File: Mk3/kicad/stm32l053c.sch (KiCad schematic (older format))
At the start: 24 parts, among them J1 CONN_01X02, P1 SWD, U1 AP2112, U2 STM32L053C8_LQFP48, U3 ADS1015, U4 EDGE_SMA, U5 RFM92/95

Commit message: Solar power
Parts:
- removed R5: R_Shunt, symbol R_Shunt
- added R?: R, symbol R
- D2: footprint (none) -> Diodes_SMD:D_0805
- J1, SC1: footprint (none) -> Pin_Headers:Pin_Header_Straight_1x02_Pitch2.54mm
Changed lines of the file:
@@
 $EndDescr
 $Comp
-L Earth #PWR5
+L Earth #PWR01
 U 1 1 58021BE1
 P 6425 1775
-F 0 "#PWR5" H 6425 1525 50  0001 C CNN
+F 0 "#PWR01" H 6425 1525 50  0001 C CNN
 F 1 "Earth" H 6425 1625 50  0001 C CNN
 F 2 "" H 6425 1775 50  0000 C CNN
@@
 $EndComp
 $Comp
-L GNDA #PWR19
+L GNDA #PWR02
 U 1 1 58021F75
 P 9325 5925
-F 0 "#PWR19" H 9325 5675 50  0001 C CNN
+F 0 "#PWR02" H 9325 5675 50  0001 C CNN
 F 1 "GNDA" H 9325 5775 50  0000 C CNN
 F 2 "" H 9325 5925 50  0000 C CNN
@@
 $EndComp
 $Comp
-L Earth #PWR20
+L Earth #PWR03
 U 1 1 58021F89
 P 9825 5925
-F 0 "#PWR20" H 9825 5675 50  0001 C CNN
+F 0 "#PWR03" H 9825 5675 50  0001 C CNN
 F 1 "Earth" H 9825 5775 50  0001 C CNN
 F 2 "" H 9825 5925 50  0000 C CNN
@@
 $EndComp
 $Comp
-L GNDA #PWR21
+L GNDA #PWR04
 U 1 1 58022154
 P 8175 5950
-F 0 "#PWR21" H 8175 5700 50  0001 C CNN
+F 0 "#PWR04" H 8175 5700 50  0001 C CNN
 F 1 "GNDA" H 8175 5800 50  0000 C CNN
 F 2 "" H 8175 5950 50  0000 C CNN
@@
 $EndComp
 $Comp
-L Earth #PWR22
+L Earth #PWR05
 U 1 1 580221FA
 P 8675 5950
-F 0 "#PWR22" H 8675 5700 50  0001 C CNN
+F 0 "#PWR05" H 8675 5700 50  0001 C CNN
 F 1 "Earth" H 8675 5800 50  0001 C CNN
 F 2 "" H 8675 5950 50  0000 C CNN
@@
 $EndComp
 $Comp
-L Earth #PWR10
+L Earth #PWR06
 U 1 1 580369A9
 P 2425 3075
-F 0 "#PWR10" H 2425 2825 50  0001 C CNN
+F 0 "#PWR06" H 2425 2825 50  0001 C CNN
 F 1 "Earth" H 2425 2925 50  0001 C CNN
 F 2 "" H 2425 3075 50  0000 C CNN
@@
 PA0
 $Comp
-L Earth #PWR7
+L Earth #PWR07
 U 1 1 58039244
 P 7525 1775
-F 0 "#PWR7" H 7525 1525 50  0001 C CNN
+F 0 "#PWR07" H 7525 1525 50  0001 C CNN
 F 1 "Earth" H 7525 1625 50  0001 C CNN
 F 2 "" H 7525 1775 50  0000 C CNN
@@
 $EndComp
 $Comp
-L Earth #PWR6
+L Earth #PWR08
 U 1 1 5803BDC8
 P 7075 1775
-F 0 "#PWR6" H 7075 1525 50  0001 C CNN
+F 0 "#PWR08" H 7075 1525 50  0001 C CNN
 F 1 "Earth" H 7075 1625 50  0001 C CNN
 F 2 "" H 7075 1775 50  0000 C CNN
@@
 $EndComp
 $Comp
-L Earth #PWR16
+L Earth #PWR09
 U 1 1 58065816
 P 7275 4950
-F 0 "#PWR16" H 7275 4700 50  0001 C CNN
+F 0 "#PWR09" H 7275 4700 50  0001 C CNN
 F 1 "Earth" H 7275 4800 50  0001 C CNN
 F 2 "" H 7275 4950 50  0000 C CNN
@@
 $EndComp
 $Comp
-L Earth #PWR11
+L Earth #PWR010
 U 1 1 58077163
 P 3575 3075
-F 0 "#PWR11" H 3575 2825 50  0001 C CNN
+F 0 "#PWR010" H 3575 2825 50  0001 C CNN
 F 1 "Earth" H 3575 2925 50  0001 C CNN
 F 2 "" H 3575 3075 50  0000 C CNN
@@
 $EndComp
 $Comp
-L Earth #PWR18
+L Earth #PWR011
 U 1 1 592DF55A
 P 2625 5475
-F 0 "#PWR18" H 2625 5225 50  0001 C CNN
+F 0 "#PWR011" H 2625 5225 50  0001 C CNN
 F 1 "Earth" H 2625 5325 50  0001 C CNN
 F 2 "" H 2625 5475 50  0000 C CNN
@@
 NoConn ~ 4150 1625
 $Comp
-L Earth #PWR8
+L Earth #PWR012
 U 1 1 592F1C89
 P 3750 1925
-F 0 "#PWR8" H 3750 1675 50  0001 C CNN
+F 0 "#PWR012" H 3750 1675 50  0001 C CNN
 F 1 "Earth" H 3750 1775 50  0001 C CNN
 F 2 "" H 3750 1925 50  0000 C CNN
@@
 RFM_RST
 $Comp
-L +3.3V #PWR1
+L +3.3V #PWR013
 U 1 1 592F43A5
 P 4450 1175
-F 0 "#PWR1" H 4450 1025 50  0001 C CNN
+F 0 "#PWR013" H 4450 1025 50  0001 C CNN
 F 1 "+3.3V" H 4450 1315 50  0000 C CNN
 F 2 "" H 4450 1175 50  0001 C CNN
@@
 $EndComp
 $Comp
-L +3.3V #PWR9
+L +3.3V #PWR014
 U 1 1 592F4BC3
 P 1925 2875
-F 0 "#PWR9" H 1925 2725 50  0001 C CNN
+F 0 "#PWR014" H 1925 2725 50  0001 C CNN
 F 1 "+3.3V" H 1925 3015 50  0000 C CNN
 F 2 "" H 1925 2875 50  0001 C CNN
@@
 $EndComp
 $Comp
-L +3.3V #PWR2
+L +3.3V #PWR015
 U 1 1 592F4E66
 P 8475 1425
-F 0 "#PWR2" H 8475 1275 50  0001 C CNN
+F 0 "#PWR015" H 8475 1275 50  0001 C CNN
 F 1 "+3.3V" H 8475 1565 50  0000 C CNN
 F 2 "" H 8475 1425 50  0001 C CNN
@@
 $EndComp
 $Comp
-L +3.3V #PWR26
+L +3.3V #PWR016
 U 1 1 592F53D7
 P 4775 6725
-F 0 "#PWR26" H 4775 6575 50  0001 C CNN
+F 0 "#PWR016" H 4775 6575 50  0001 C CNN
 F 1 "+3.3V" H 4775 6865 50  0000 C CNN
 F 2 "" H 4775 6725 50  0001 C CNN
@@
 $EndComp
 $Comp
-L +3.3V #PWR3
+L +3.3V #PWR017
 U 1 1 592F54CD
 P 7525 1475
-F 0 "#PWR3" H 7525 1325 50  0001 C CNN
+F 0 "#PWR017" H 7525 1325 50  0001 C CNN
 F 1 "+3.3V" H 7525 1615 50  0000 C CNN
 F 2 "" H 7525 1475 50  0001 C CNN
@@
 NoConn ~ 3400 7025
 $Comp
-L Earth #PWR27
+L Earth #PWR018
 U 1 1 592F7C8A
 P 4775 7025
-F 0 "#PWR27" H 4775 6775 50  0001 C CNN
+F 0 "#PWR018" H 4775 6775 50  0001 C CNN
 F 1 "Earth" H 4775 6875 50  0001 C CNN
 F 2 "" H 4775 7025 50  0000 C CNN
@@
 $EndComp
 $Comp
-L Earth #PWR23
+L Earth #PWR019
 U 1 1 592F7CF0
 P 2750 6425
-F 0 "#PWR23" H 2750 6175 50  0001 C CNN
+F 0 "#PWR019" H 2750 6175 50  0001 C CNN
 F 1 "Earth" H 2750 6275 50  0001 C CNN
 F 2 "" H 2750 6425 50  0000 C CNN
@@
 $EndComp
 $Comp
-L Earth #PWR28
+L Earth #PWR020
 U 1 1 592F7EE4
 P 3225 7125
-F 0 "#PWR28" H 3225 6875 50  0001 C CNN
+F 0 "#PWR020" H 3225 6875 50  0001 C CNN
 F 1 "Earth" H 3225 6975 50  0001 C CNN
 F 2 "" H 3225 7125 50  0000 C CNN
@@
 $EndComp
 $Comp
-L Earth #PWR24
+L Earth #PWR021
 U 1 1 592F80DC
 P 1300 6575
-F 0 "#PWR24" H 1300 6325 50  0001 C CNN
+F 0 "#PWR021" H 1300 6325 50  0001 C CNN
 F 1 "Earth" H 1300 6425 50  0001 C CNN
 F 2 "" H 1300 6575 50  0000 C CNN
@@
 $EndComp
 $Comp
-L Earth #PWR25
+L Earth #PWR022
 U 1 1 592F814F
 P 2050 6600
-F 0 "#PWR25" H 2050 6350 50  0001 C CNN
+F 0 "#PWR022" H 2050 6350 50  0001 C CNN
 F 1 "Earth" H 2050 6450 50  0001 C CNN
 F 2 "" H 2050 6600 50  0000 C CNN
@@
 $EndComp
 $Comp
-L Earth #PWR17
+L Earth #PWR023
 U 1 1 59301904
 P 3525 5175
-F 0 "#PWR17" H 3525 4925 50  0001 C CNN
+F 0 "#PWR023" H 3525 4925 50  0001 C CNN
 F 1 "Earth" H 3525 5025 50  0001 C CNN
 F 2 "" H 3525 5175 50  0000 C CNN
@@
 $EndComp
 $Comp
-L Earth #PWR15
+L Earth #PWR024
 U 1 1 593024E3
 P 3425 4475
-F 0 "#PWR15" H 3425 4225 50  0001 C CNN
+F 0 "#PWR024" H 3425 4225 50  0001 C CNN
 F 1 "Earth" H 3425 4325 50  0001 C CNN
 F 2 "" H 3425 4475 50  0000 C CNN
@@
 $EndComp
 $Comp
-L +3.3V #PWR12
+L +3.3V #PWR025
 U 1 1 59303669
 P 2625 4175
-F 0 "#PWR12" H 2625 4025 50  0001 C CNN
+F 0 "#PWR025" H 2625 4025 50  0001 C CNN
 F 1 "+3.3V" H 2625 4315 50  0000 C CNN
 F 2 "" H 2625 4175 50  0001 C CNN
@@
 $EndComp
 $Comp
-L +3.3V #PWR13
+L +3.3V #PWR026
 U 1 1 59303771
 P 3825 4175
-F 0 "#PWR13" H 3825 4025 50  0001 C CNN
+F 0 "#PWR026" H 3825 4025 50  0001 C CNN
 F 1 "+3.3V" H 3825 4315 50  0000 C CNN
 F 2 "" H 3825 4175 50  0001 C CNN
@@
 $EndComp
 $Comp
-L Earth #PWR4
+L Earth #PWR027
 U 1 1 59316863
 P 2600 1675
-F 0 "#PWR4" H 2600 1425 50  0001 C CNN
+F 0 "#PWR027" H 2600 1425 50  0001 C CNN
 F 1 "Earth" H 2600 1525 50  0001 C CNN
 F 2 "" H 2600 1675 50  0000 C CNN
@@
 F 0 "SC1" V 1925 1200 50  0000 L CNN
 F 1 "Solar_Cells" V 1650 850 50  0000 L CNN
-F 2 "" V 1800 1335 50  0001 C CNN
+F 2 "Pin_Headers:Pin_Header_Straight_1x02_Pitch2.54mm" V 1800 1335 50  0001 C CNN
 F 3 "" V 1800 1335 50  0001 C CNN
 	1    1800 1275
@@
 F 0 "D2" H 2300 1375 50  0000 C CNN
 F 1 "D_Schottky" H 2300 1175 50  0000 C CNN
-F 2 "" H 2300 1275 50  0001 C CNN
+F 2 "Diodes_SMD:D_0805" H 2300 1275 50  0001 C CNN
 F 3 "" H 2300 1275 50  0001 C CNN
 	1    2300 1275
@@
 $EndComp
 $Comp
-L R_Shunt R5
-U 1 1 59328FA3
-P 1500 4325
-F 0 "R5" V 1325 4325 50  0000 C CNN
-F 1 "R_Shunt" V 1400 4325 50  0000 C CNN
-F 2 "" V 1430 4325 50  0001 C CNN
-F 3 "" H 1500 4325 50  0001 C CNN
-	1    1500 4325
-	0    1    1    0
-$EndComp
-$Comp
-L Earth #PWR14
+L Earth #PWR028
 U 1 1 593290F6
 P 1150 4325
-F 0 "#PWR14" H 1150 4075 50  0001 C CNN
+F 0 "#PWR028" H 1150 4075 50  0001 C CNN
 F 1 "Earth" H 1150 4175 50  0001 C CNN
 F 2 "" H 1150 4325 50  0000 C CNN
@@
 Connection ~ 8575 1625
 Wire Wire Line
-	6725 1475 6425 1475
+	6425 1475 6725 1475
 Wire Wire Line
 	6725 1775 6425 1775
@@
 F 0 "J1" H 1725 5275 50  0000 C CNN
 F 1 "CONN_01X02" V 1825 5125 50  0000 C CNN
-F 2 "" H 1725 5125 50  0001 C CNN
+F 2 "Pin_Headers:Pin_Header_Straight_1x02_Pitch2.54mm" H 1725 5125 50  0001 C CNN
 F 3 "" H 1725 5125 50  0001 C CNN
 	1    1725 5125
@@
 SOLAR
 Wire Wire Line
-	1700 4325 2000 4325
-Wire Wire Line
-	1300 4325 1150 4325
-Wire Wire Line
-	1600 4475 1600 4775
-Wire Wire Line
-	1600 4775 1925 4775
-Wire Wire Line
-	1925 4875 1400 4875
-Wire Wire Line
-	1400 4875 1400 4475
+	1650 4325 2000 4325
+Wire Wire Line
+	1350 4325 1150 4325
+Wire Wire Line
+	1650 4325 1650 4775
+Wire Wire Line
+	1650 4775 1925 4775
+Wire Wire Line
+	1350 4875 1925 4875
+Wire Wire Line
+	1350 4325 1350 4875
 Text Label 1275 1275 0    60   ~ 0
 SOLAR
@@
 	1    0    0    -1
 $EndComp
+$Comp
+L R R?
+U 1 1 59340973
+P 1500 4325
+F 0 "R?" V 1580 4325 50  0000 C CNN
+F 1 "R" V 1500 4325 50  0000 C CNN
+F 2 "" V 1430 4325 50  0001 C CNN
+F 3 "" H 1500 4325 50  0001 C CNN
+	1    1500 4325
+	0    1    1    0
+$EndComp
 $EndSCHEMATC

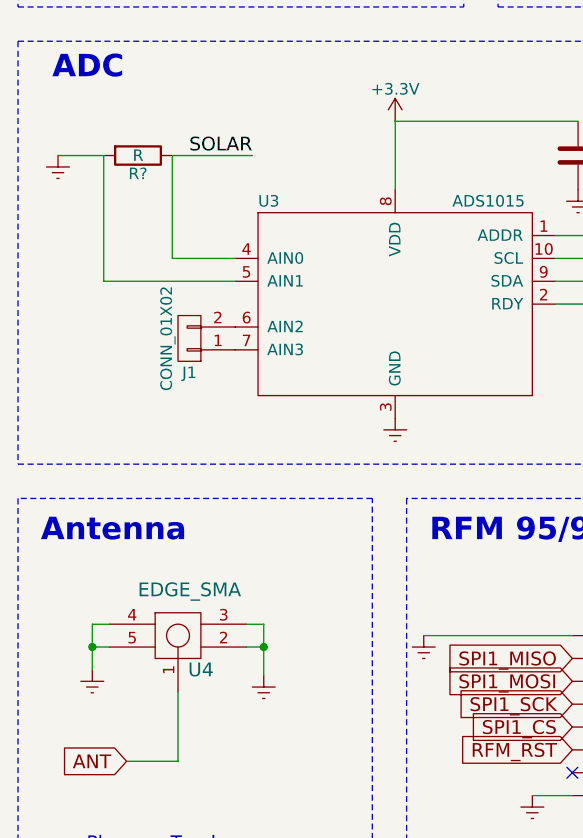
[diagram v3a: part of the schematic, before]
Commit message: UFL SMA antenna connector
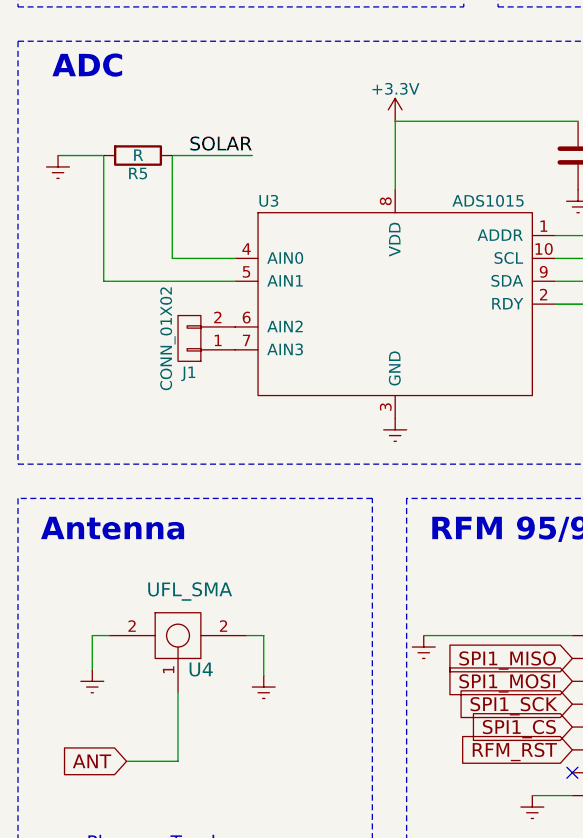
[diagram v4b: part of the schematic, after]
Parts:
- removed U4: EDGE_SMA, kicad:EDGE_SMA_5, symbol EDGE_SMA
- added U4: UFL_SMA, w_conn_rf:coaxial_u.fl-r-smt-1, symbol UFL_SMA
- R5: renamed from R?; footprint (none) -> Resistors_SMD:R_1206_HandSoldering
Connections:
- wire segments 73 -> 71
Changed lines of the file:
@@
 Place on Top layer
-$Comp
-L EDGE_SMA U4
-U 1 1 592DE9B4
-P 1725 6425
-F 0 "U4" H 1775 6275 60  0000 C CNN
-F 1 "EDGE_SMA" H 1725 6625 60  0000 C CNN
-F 2 "kicad:EDGE_SMA_5" H 1725 6425 60  0001 C CNN
-F 3 "" H 1725 6425 60  0001 C CNN
-F 4 "SMA RF Connector" H 1725 6425 60  0001 C CNN "DESC"
-F 5 "molex" H 1725 6425 60  0001 C CNN "MFG_NAME"
-F 6 "0732511150" H 1725 6425 60  0001 C CNN "MPN"
-	1    1725 6425
-	1    0    0    -1
-$EndComp
 $Comp
 L Earth #PWR011
@@
 Connection ~ 8325 1625
 Wire Wire Line
-	1300 6375 1300 6575
-Wire Wire Line
-	1300 6475 1375 6475
-Wire Wire Line
-	1300 6375 1375 6375
-Connection ~ 1300 6475
-Wire Wire Line
-	1975 6375 2050 6375
-Wire Wire Line
-	2050 6375 2050 6600
-Wire Wire Line
-	1975 6475 2050 6475
-Connection ~ 2050 6475
-Wire Wire Line
 	3225 7125 3400 7125
 Wire Wire Line
@@
 $EndComp
 $Comp
-L R R?
+L R R5
 U 1 1 59340973
 P 1500 4325
-F 0 "R?" V 1580 4325 50  0000 C CNN
+F 0 "R5" V 1580 4325 50  0000 C CNN
 F 1 "R" V 1500 4325 50  0000 C CNN
-F 2 "" V 1430 4325 50  0001 C CNN
+F 2 "Resistors_SMD:R_1206_HandSoldering" V 1430 4325 50  0001 C CNN
 F 3 "" H 1500 4325 50  0001 C CNN
 	1    1500 4325
 	0    1    1    0
 $EndComp
+$Comp
+L UFL_SMA U4
+U 1 1 5934043A
+P 1725 6425
+F 0 "U4" H 1775 6275 60  0000 C CNN
+F 1 "UFL_SMA" H 1725 6625 60  0000 C CNN
+F 2 "w_conn_rf:coaxial_u.fl-r-smt-1" H 1725 6425 60  0001 C CNN
+F 3 "" H 1725 6425 60  0001 C CNN
+	1    1725 6425
+	1    0    0    -1
+$EndComp
+Wire Wire Line
+	2050 6600 2050 6425
+Wire Wire Line
+	2050 6425 1975 6425
+Wire Wire Line
+	1300 6575 1300 6425
+Wire Wire Line
+	1300 6425 1375 6425
 $EndSCHEMATC

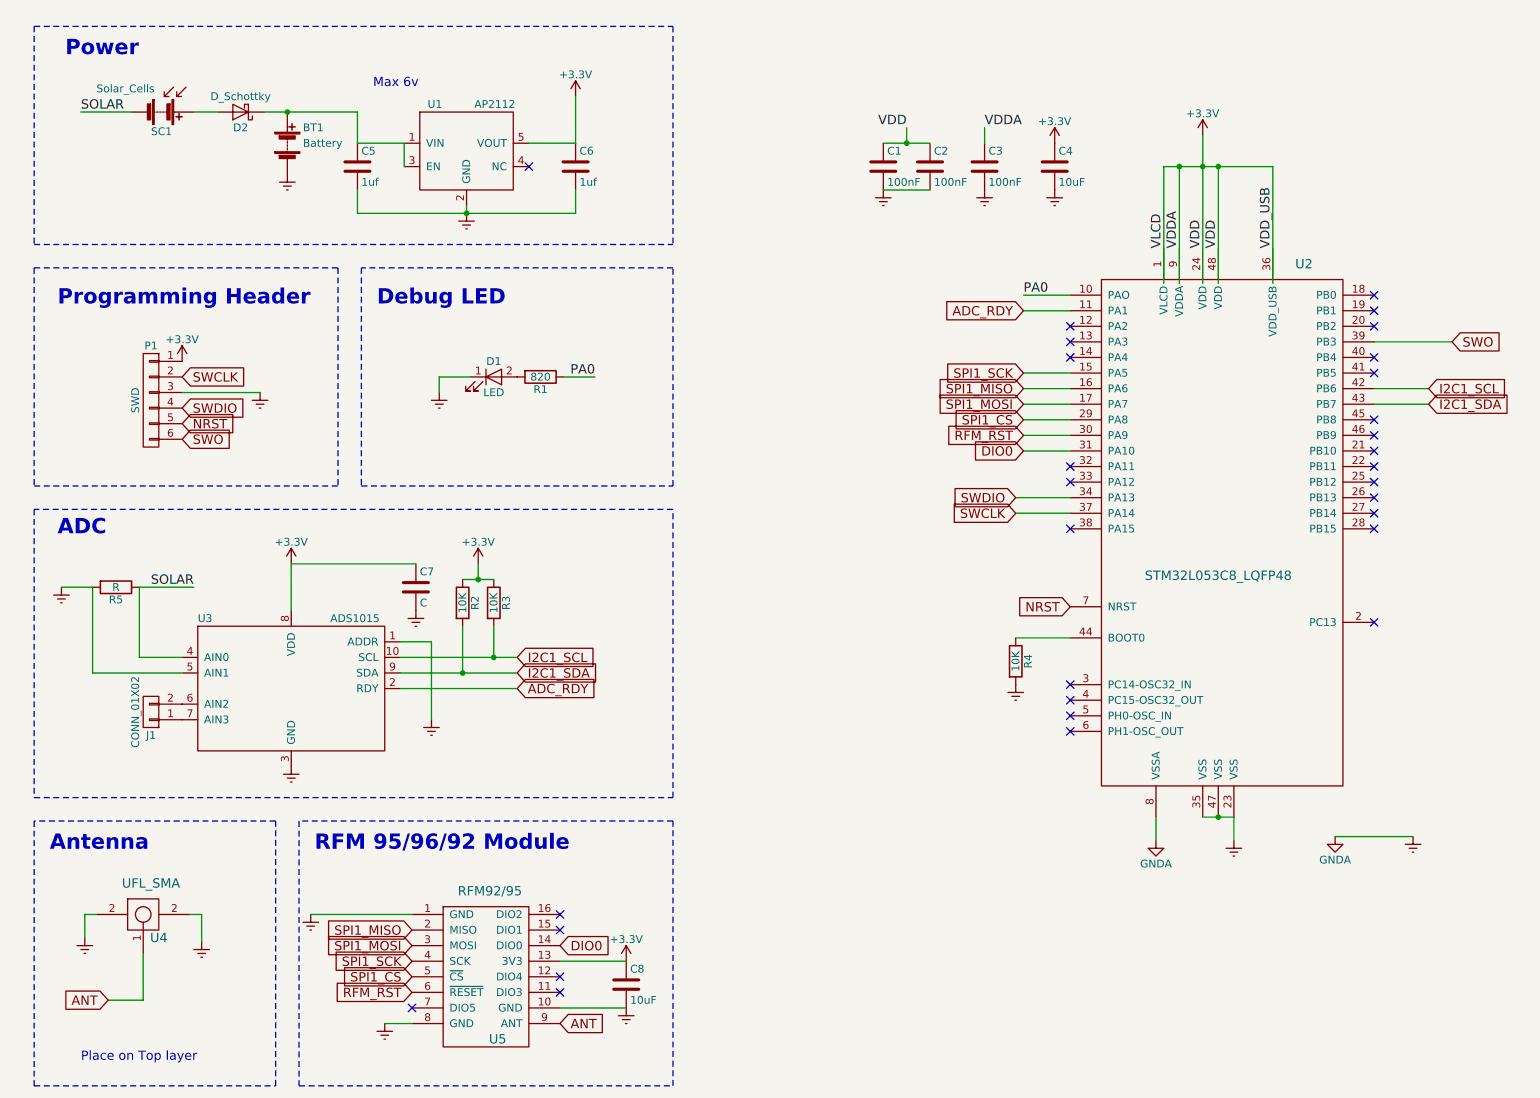
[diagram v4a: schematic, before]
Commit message: Compact layout + voltage dividers
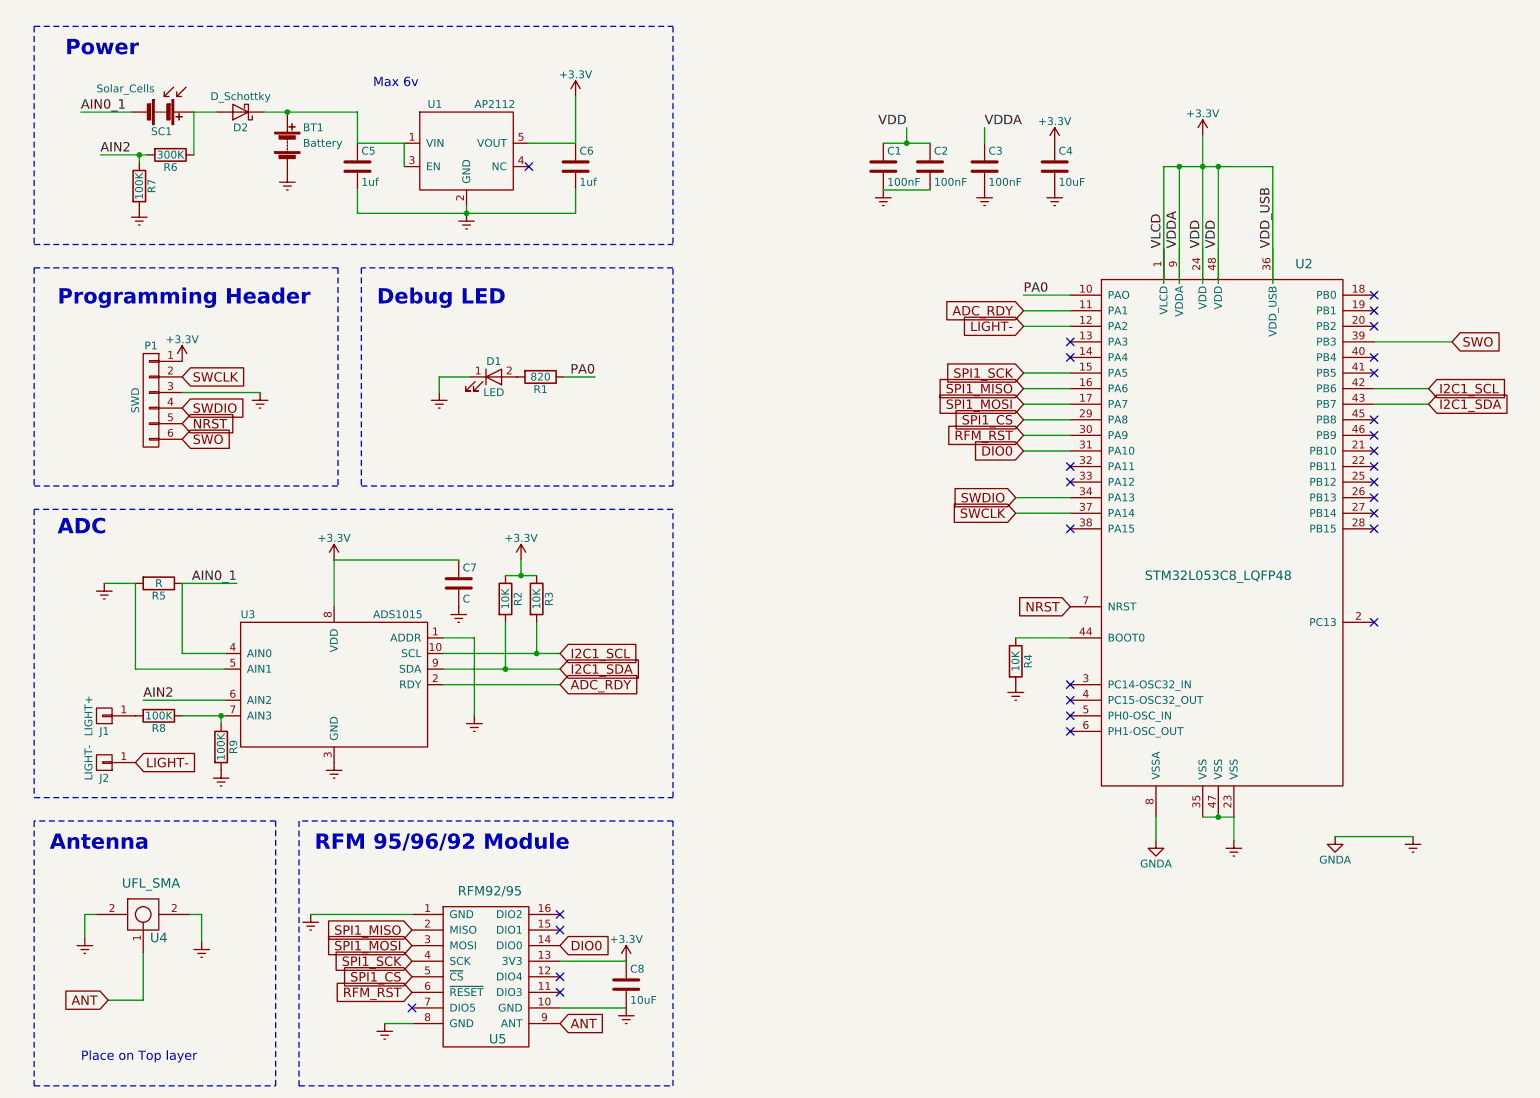
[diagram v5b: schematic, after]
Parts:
- removed J1: CONN_01X02, Pin_Headers:Pin_Header_Straight_1x02_Pitch2.54mm, symbol CONN_01X02
- added J1: LIGHT+, Pin_Headers:Pin_Header_Straight_1x01, symbol CONN_01X01
- added J2: LIGHT-, Pin_Headers:Pin_Header_Straight_1x01, symbol CONN_01X01
- added R6: 300K, Resistors_SMD:R_0805_HandSoldering, symbol R
- added R7, R8, R9: 100K, Resistors_SMD:R_0805_HandSoldering, symbol R
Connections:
- net labels added: AIN0_1, AIN2, LIGHT-
- net labels removed: SOLAR
- wire segments 71 -> 78
- no-connect marks 30 -> 29
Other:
- moved on the sheet: C7, R2, R3, R5, U3

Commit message: Battery box layout
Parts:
- BT1: footprint Pin_Headers:Pin_Header_Straight_1x02_Pitch2.54mm -> theapi:BatteryBox
- J1, J2: footprint Pin_Headers:Pin_Header_Straight_1x01 -> Pin_Headers:Pin_Header_Straight_1x01_Pitch2.54mm
- P1: footprint Pin_Headers:Pin_Header_Straight_1x06_Pitch2.54mm -> theapi:Pin_Header_Straight_1x06_Pitch2.54mm
- U4: footprint w_conn_rf:coaxial_u.fl-r-smt-1 -> theapi:coaxial_u.fl-r-smt-1
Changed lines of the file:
@@
 F 0 "P1" H 1725 3475 50  0000 C CNN
 F 1 "SWD" V 1825 3125 50  0000 C CNN
-F 2 "Pin_Headers:Pin_Header_Straight_1x06_Pitch2.54mm" H 1725 3125 50  0001 C CNN
+F 2 "theapi:Pin_Header_Straight_1x06_Pitch2.54mm" H 1725 3125 50  0001 C CNN
 F 3 "" H 1725 3125 50  0000 C CNN
 	1    1725 3125
@@
 F 0 "BT1" H 2700 1575 50  0000 L CNN
 F 1 "Battery" H 2700 1475 50  0000 L CNN
-F 2 "Pin_Headers:Pin_Header_Straight_1x02_Pitch2.54mm" V 2600 1535 50  0001 C CNN
+F 2 "theapi:BatteryBox" V 2600 1535 50  0001 C CNN
 F 3 "" V 2600 1535 50  0001 C CNN
 	1    2600 1475
@@
 F 0 "U4" H 1775 6275 60  0000 C CNN
 F 1 "UFL_SMA" H 1725 6625 60  0000 C CNN
-F 2 "w_conn_rf:coaxial_u.fl-r-smt-1" H 1725 6425 60  0001 C CNN
+F 2 "theapi:coaxial_u.fl-r-smt-1" H 1725 6425 60  0001 C CNN
 F 3 "" H 1725 6425 60  0001 C CNN
 	1    1725 6425
@@
 F 0 "J1" H 1425 5250 50  0000 C CNN
 F 1 "LIGHT+" V 1525 5150 50  0000 C CNN
-F 2 "Pin_Headers:Pin_Header_Straight_1x01" H 1425 5150 50  0001 C CNN
+F 2 "Pin_Headers:Pin_Header_Straight_1x01_Pitch2.54mm" H 1425 5150 50  0001 C CNN
 F 3 "" H 1425 5150 50  0001 C CNN
 	1    1425 5150
@@
 F 0 "J2" H 1425 5550 50  0000 C CNN
 F 1 "LIGHT-" V 1525 5450 50  0000 C CNN
-F 2 "Pin_Headers:Pin_Header_Straight_1x01" H 1425 5450 50  0001 C CNN
+F 2 "Pin_Headers:Pin_Header_Straight_1x01_Pitch2.54mm" H 1425 5450 50  0001 C CNN
 F 3 "" H 1425 5450 50  0001 C CNN
 	1    1425 5450
